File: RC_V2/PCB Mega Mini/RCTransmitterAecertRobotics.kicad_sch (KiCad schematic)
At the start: 39 parts, among them K1 KCD1 Power Switch

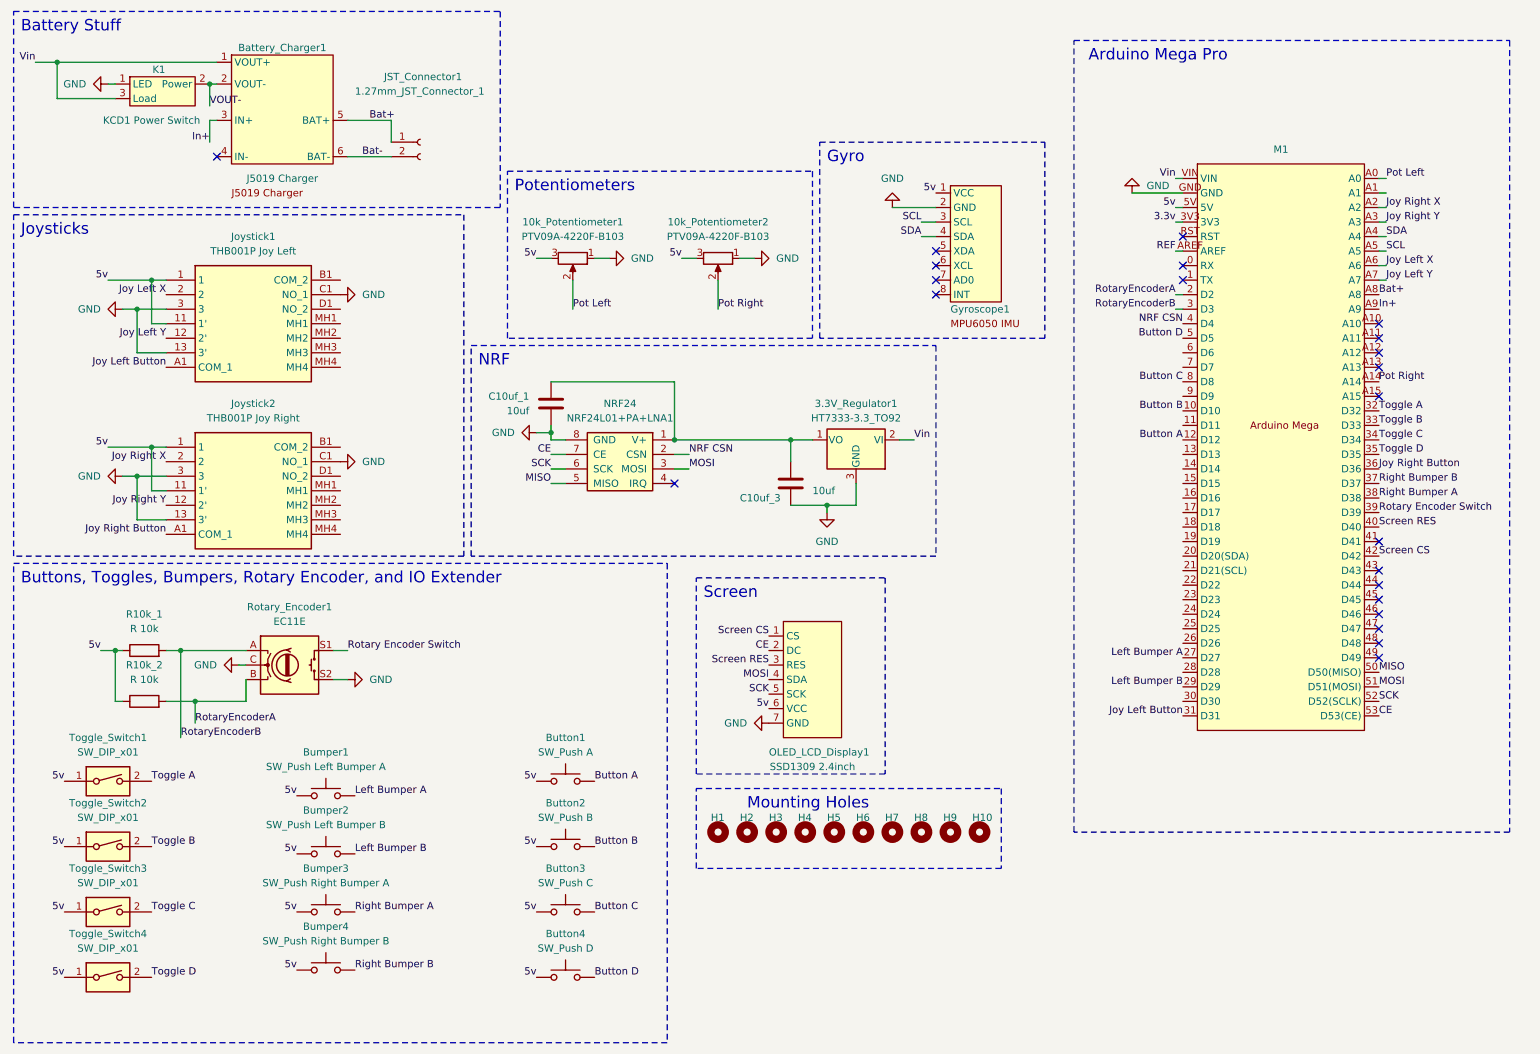
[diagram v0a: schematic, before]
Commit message: rcv2 pcb finished, added new gait
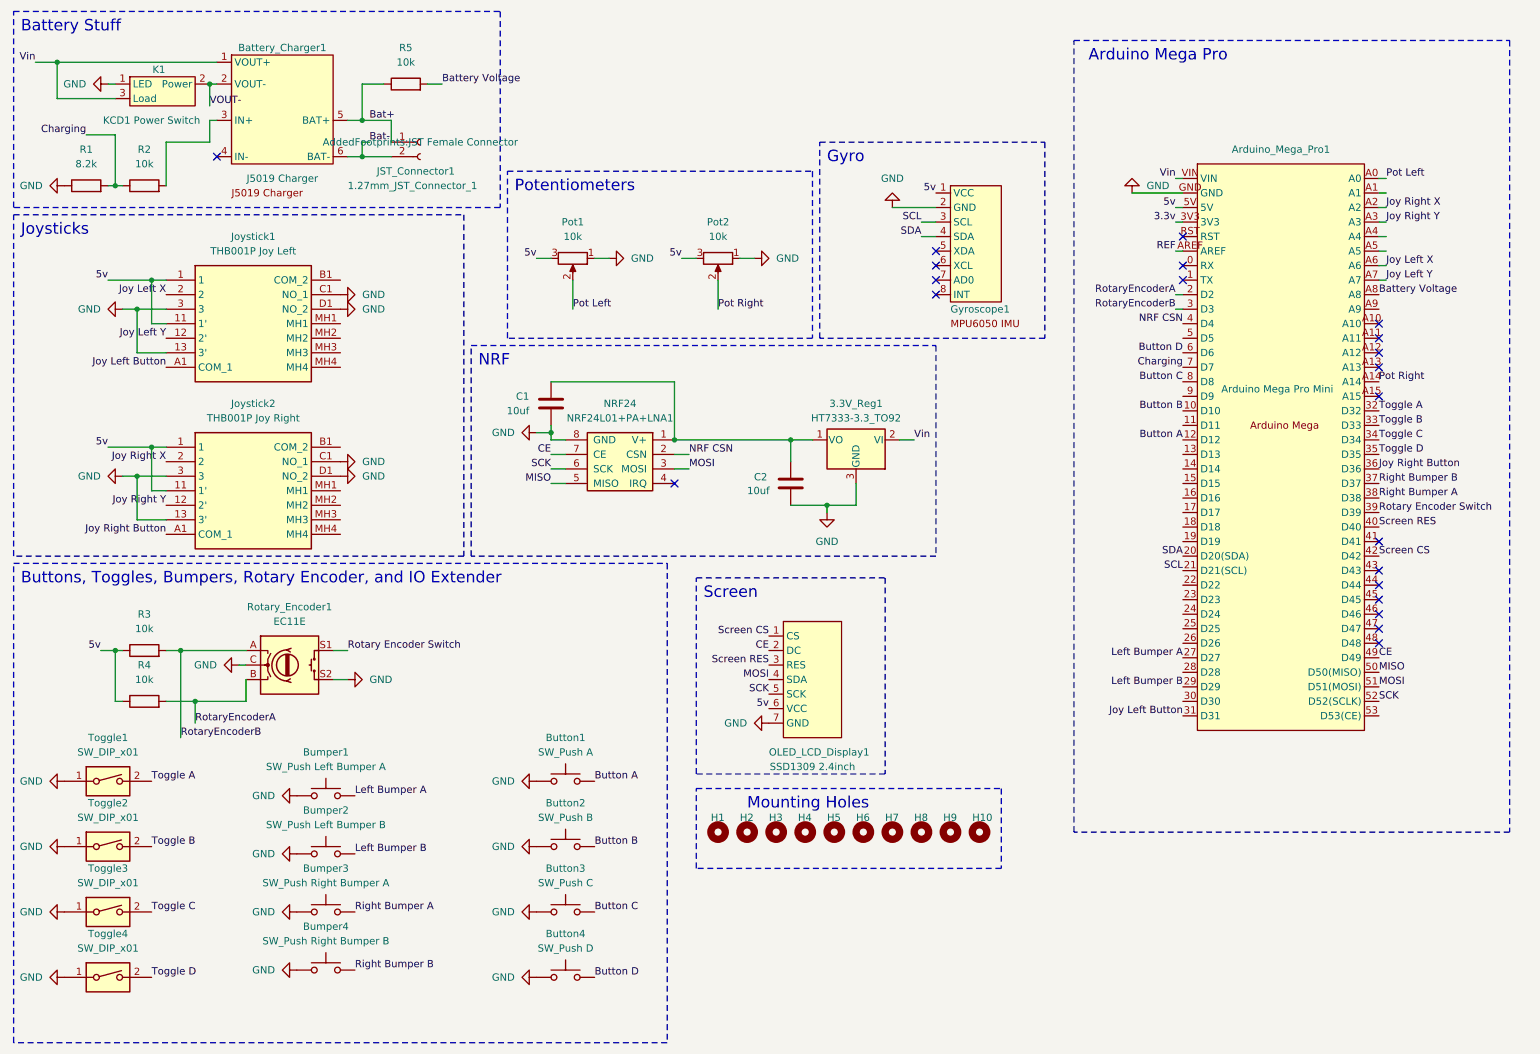
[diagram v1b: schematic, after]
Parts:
- added R1: 8.2k, Resistor_THT:R_Axial_DIN0207_L6.3mm_D2.5mm_P7.62mm_Horizontal, symbol Device:R
- added R2, R5: 10k, Resistor_THT:R_Axial_DIN0207_L6.3mm_D2.5mm_P7.62mm_Horizontal, symbol Device:R
- Arduino_Mega_Pro1: renamed from M1; value ~ -> Arduino Mega Pro Mini
- JST_Connector1: footprint Connector_PinSocket_1.27mm:PinSocket_1x02_P1.27mm_Vertical -> AddedFootprints:JST Female Connector
- Pot1: renamed from 10k_Potentiometer1; value PTV09A-4220F-B103 -> 10k; Part Number (none) -> PTV09A-4220F-B103
- Pot2: renamed from 10k_Potentiometer2; value PTV09A-4220F-B103 -> 10k; Part Number (none) -> PTV09A-4220F-B103
- R3: renamed from R10k_1; value R 10k -> 10k
- R4: renamed from R10k_2; value R 10k -> 10k
- renumbered 3.3V_Regulator1 to 3.3V_Reg1, C10uf_1 to C1, C10uf_3 to C2, Toggle_Switch1 to Toggle1, Toggle_Switch2 to Toggle2, Toggle_Switch3 to Toggle3, Toggle_Switch4 to Toggle4
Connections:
- net 5v: no longer Bumper1.1, Bumper2.1, Bumper3.1, Bumper4.1, Button1.1, Button2.1, Button3.1, Button4.1, Toggle1.1, Toggle2.1, Toggle3.1, Toggle4.1
- net Bat+: now also R5.1; no longer Arduino_Mega_Pro1.A8
- net Button D: now also Arduino_Mega_Pro1.6 (D6); no longer Arduino_Mega_Pro1.5 (D5)
- net CE: now also Arduino_Mega_Pro1.49 (D49); no longer Arduino_Mega_Pro1.53 (D53(CE))
- net GND: now also Bumper1.1, Bumper2.1, Bumper3.1, Bumper4.1, Button1.1, Button2.1, Button3.1, Button4.1, Joystick1.D1 (NO_2), Joystick2.D1 (NO_2), Toggle1.1, Toggle2.1, Toggle3.1, Toggle4.1, R1.1
- net SCL: now also Arduino_Mega_Pro1.21 (D21(SCL)); no longer Arduino_Mega_Pro1.A5
- net SDA: now also Arduino_Mega_Pro1.20 (D20(SDA)); no longer Arduino_Mega_Pro1.A4
- net Charging: now reaches Arduino_Mega_Pro1.7 (D7)
- net Charging: now also R1.2, R2.1
- net In+: no longer names the net of Arduino_Mega_Pro1.A9
- net In+: no longer Battery_Charger1.3 (IN+)
- new net: Battery_Charger1.3 (IN+), R2.2
- new net Battery Voltage: Arduino_Mega_Pro1.A8, R5.2
- no-connect marks 22 -> 21

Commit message: updated code pins and pcb
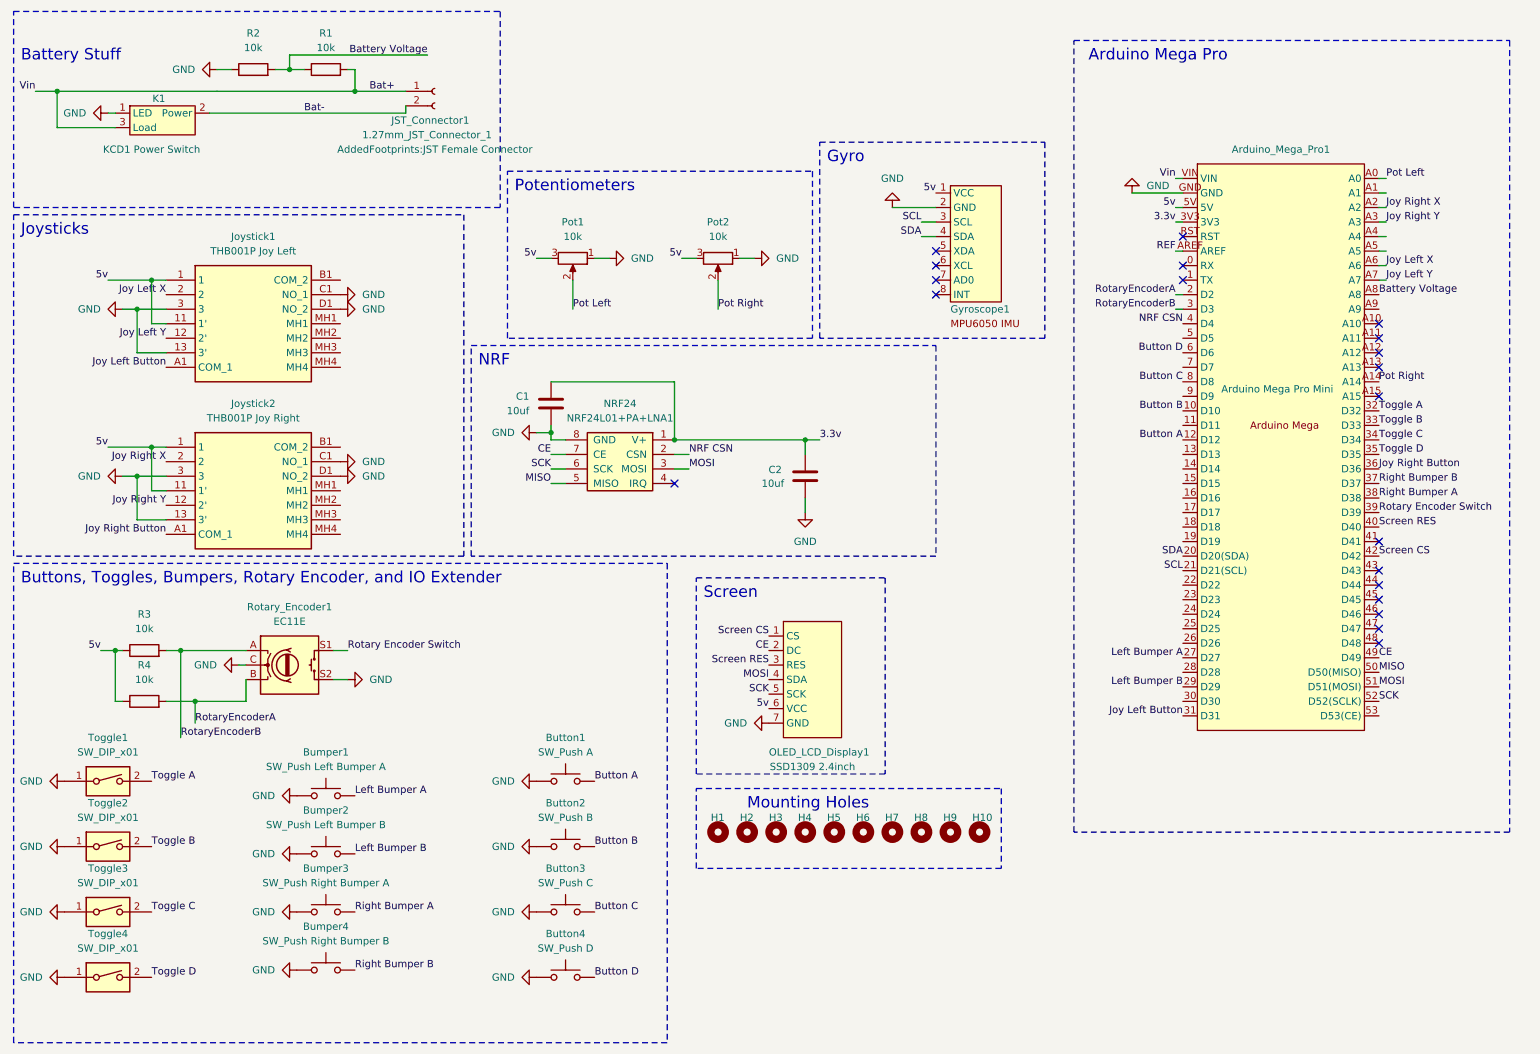
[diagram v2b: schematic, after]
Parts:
- removed 3.3V_Reg1: HT7333-3.3_TO92, Package_TO_SOT_THT:TO-92_Inline, symbol Regulator_Linear:LM2936-3.3_TO92
- removed Battery_Charger1: J5019 Charger, AddedFootprints:J5019 Charger, symbol Modules:J5019_Charger
- removed R5: 10k, Resistor_THT:R_Axial_DIN0207_L6.3mm_D2.5mm_P7.62mm_Horizontal, symbol Device:R
- R1: value 8.2k -> 10k
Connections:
- net VOUT- is gone; now on net Bat-: K1.2 (Power)
- net Vin is gone; now on net Bat+: Arduino_Mega_Pro1.VIN, K1.3 (Load)
- net 3.3v: now also C1.1, C2.1, NRF24.1 (V+)
- net Bat+: now also R1.2
- net Battery Voltage: now also R1.1, R2.2
- net GND: now also R2.1; no longer R1.1
- removed net Charging: Arduino_Mega_Pro1.7 (D7), R1.2, R2.1
- no-connect marks 21 -> 20
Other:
- moved on the sheet: C2, JST_Connector1, K1

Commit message: Updated PCB, Made screen spacer and backplate
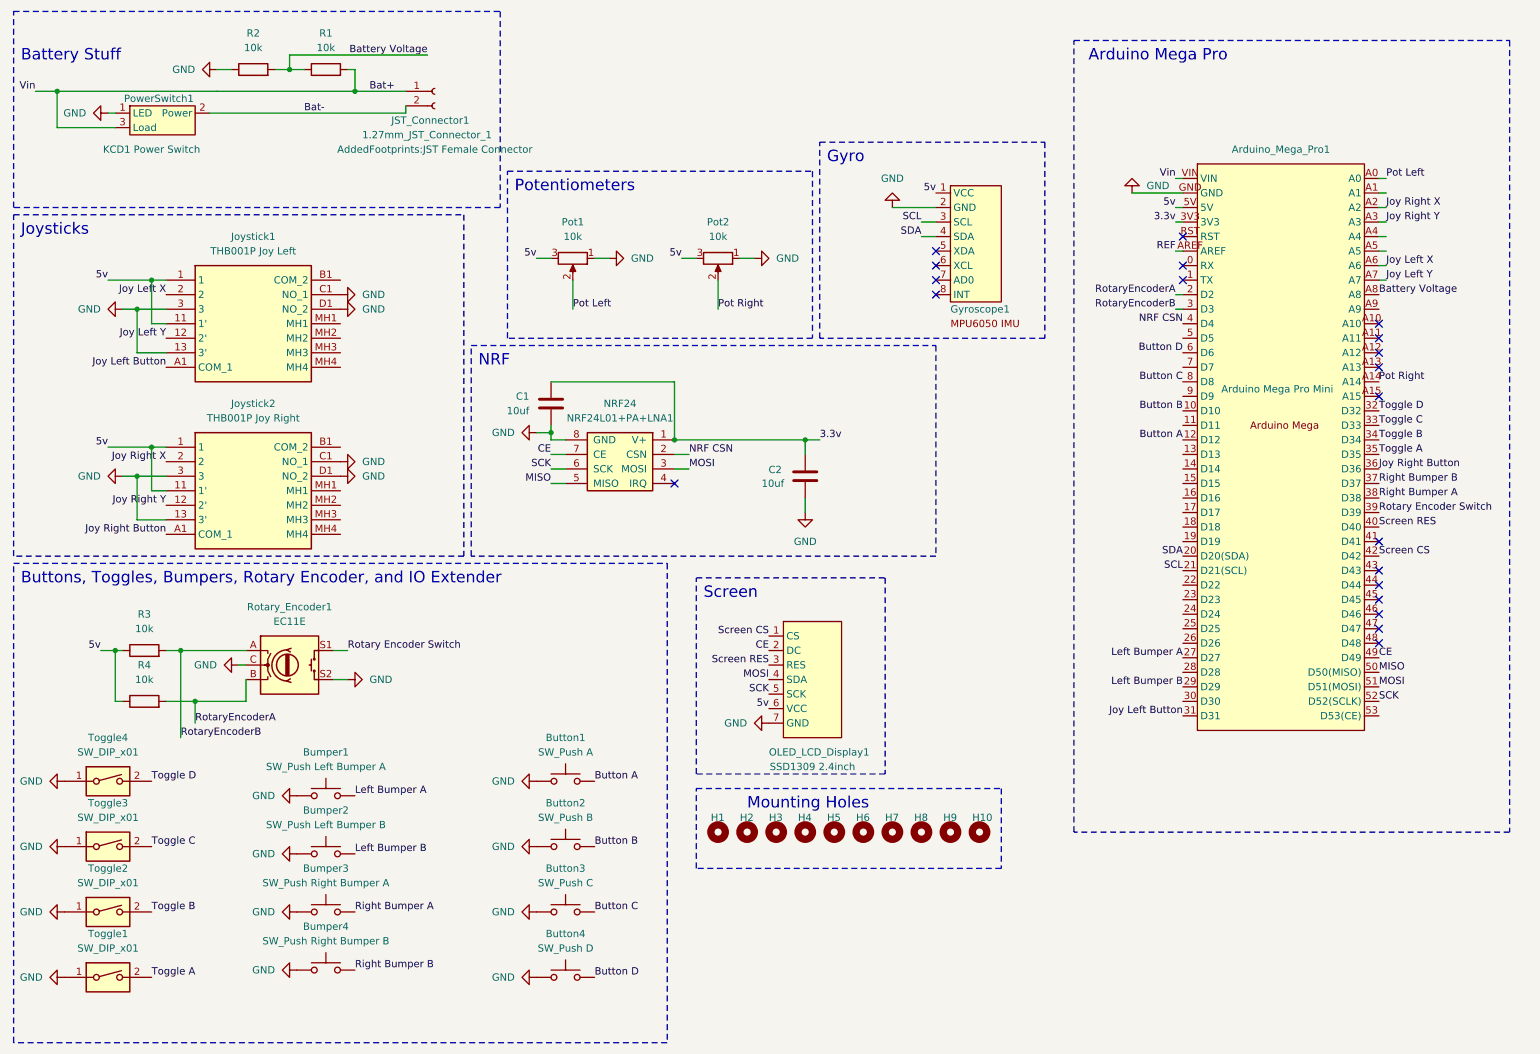
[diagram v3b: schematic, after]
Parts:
- Bumper1, Bumper2, Bumper3, Bumper4: footprint Connector_PinHeader_2.00mm:PinHeader_1x02_P2.00mm_Vertical -> AddedFootprints:Bumper Pads
- renumbered H8 to H10, H9 to H5, H10 to H7, H5 to H8, H7 to H9, K1 to PowerSwitch1, Toggle4 to Toggle1, Toggle3 to Toggle2, Toggle2 to Toggle3, Toggle1 to Toggle4
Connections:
- net Toggle A: now also Arduino_Mega_Pro1.35 (D35), Toggle1.2; no longer Arduino_Mega_Pro1.32 (D32), Toggle4.2
- net Toggle B: now also Arduino_Mega_Pro1.34 (D34), Toggle2.2; no longer Arduino_Mega_Pro1.33 (D33), Toggle3.2
- net Toggle C: now also Arduino_Mega_Pro1.33 (D33), Toggle3.2; no longer Arduino_Mega_Pro1.34 (D34), Toggle2.2
- net Toggle D: now also Arduino_Mega_Pro1.32 (D32), Toggle4.2; no longer Arduino_Mega_Pro1.35 (D35), Toggle1.2
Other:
- moved on the sheet: H10, H5, H7, H8, H9
